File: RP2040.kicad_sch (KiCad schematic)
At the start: 26 parts, among them J3 Conn_01x02, J6 USB_B_Micro, U2 XC6206P332MR, U6 W25Q128JVS, U7 RP2040, Y1 X322512MSB4SI

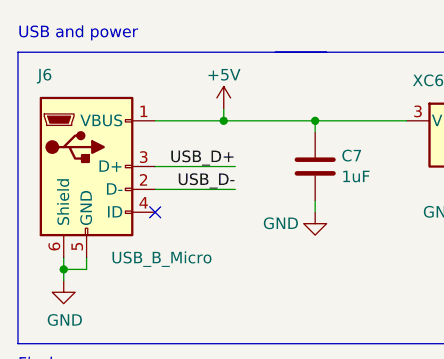
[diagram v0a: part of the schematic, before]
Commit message: Cleanup silkscreen and version/date
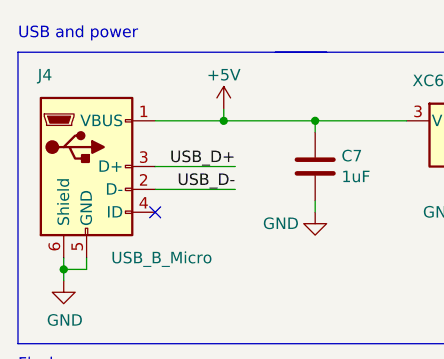
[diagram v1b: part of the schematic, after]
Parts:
- renumbered J6 to J4
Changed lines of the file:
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@@
   (paper "A4")
   (title_block
-    (date "${DATE}")
-    (rev "${VERSION}")
+    (date "${date}")
+    (rev "${version}")
   )
   (junction (at 215.9 20.32) (diameter 0) (color 0 0 0 0)
@@
   (symbol (lib_id "Connector:USB_B_Micro") (at 22.225 29.845 0) (unit 1)
     (in_bom yes) (on_board yes)
-    (property "Reference" "J6" (id 0) (at 18.415 19.685 0)
+    (property "Reference" "J4" (id 0) (at 18.415 19.685 0)
       (effects (font (size 1.27 1.27)) (justify right))
     )

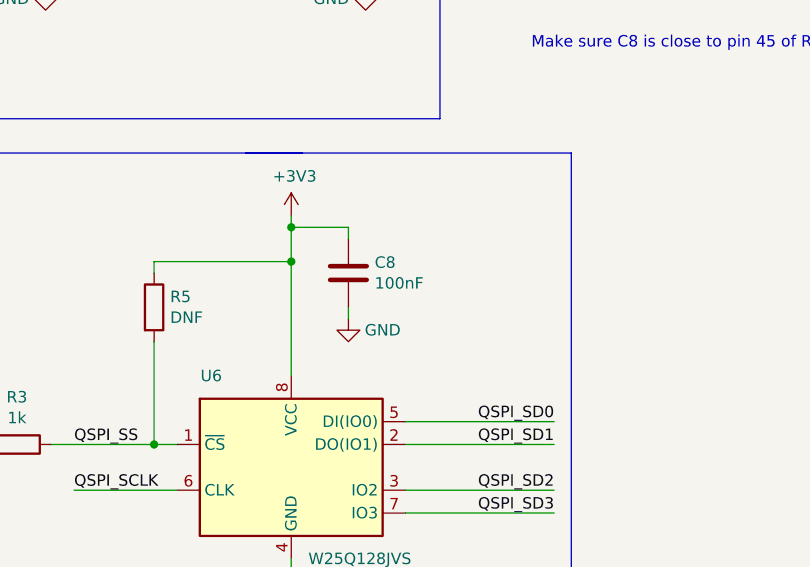
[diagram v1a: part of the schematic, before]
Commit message: Silkscreen and date/version stuff
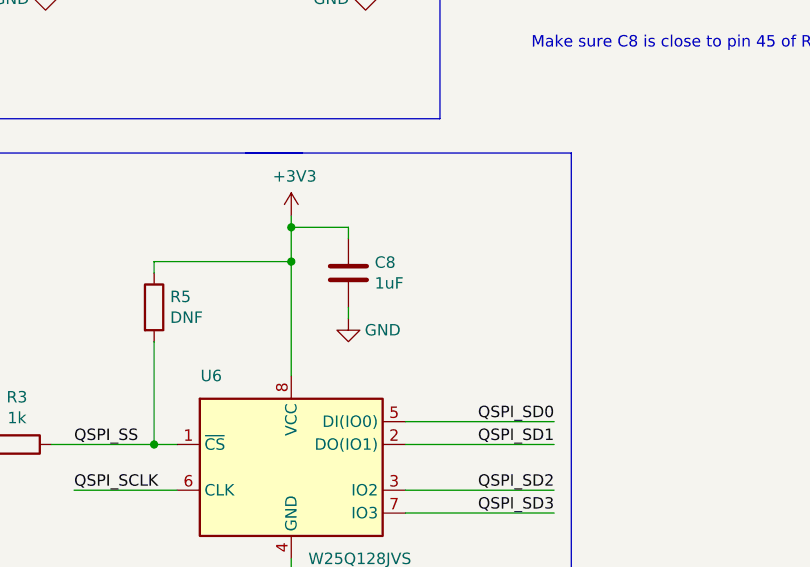
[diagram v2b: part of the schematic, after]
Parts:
- C10, C11, C12, C13, C15, C16, C17, C18, C19, C20: LCSC (none) -> C52923
- C7, C9: footprint Capacitor_SMD:C_0603_1608Metric -> Custom_Footprints:Perfect_0402; JLC 0603 -> 0402; LCSC C19702 -> C52923
- C8: value 100nF -> 1uF; LCSC C1525 -> C52923
- U6: JLC SOIC-8_5.3x5.3x1.27P -> SOIC-8-208mil
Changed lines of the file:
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@@
   (paper "A4")
   (title_block
-    (date "${date}")
-    (rev "${version}")
+    (date "${DATE}")
+    (rev "${VERSION}")
   )
   (junction (at 215.9 20.32) (diameter 0) (color 0 0 0 0)
@@
       (effects (font (size 1.27 1.27)) hide)
     )
-    (property "LCSC" "" (id 5) (at 149.86 25.4 0)
+    (property "LCSC" "C52923" (id 5) (at 149.86 25.4 0)
       (effects (font (size 1.27 1.27)) hide)
     )
@@
       (effects (font (size 1.27 1.27)) hide)
     )
-    (property "LCSC" "" (id 5) (at 149.86 40.64 0)
+    (property "LCSC" "C52923" (id 5) (at 149.86 40.64 0)
       (effects (font (size 1.27 1.27)) hide)
     )
@@
       (effects (font (size 1.27 1.27)) (justify left))
     )
-    (property "Footprint" "Capacitor_SMD:C_0603_1608Metric" (id 2) (at 84.1502 33.655 0)
+    (property "Footprint" "Custom_Footprints:Perfect_0402" (id 2) (at 84.1502 33.655 0)
       (effects (font (size 1.27 1.27)) hide)
     )
@@
       (effects (font (size 1.27 1.27)) hide)
     )
-    (property "JLC" "0603" (id 4) (at 83.185 29.845 0)
-      (effects (font (size 1.27 1.27)) hide)
-    )
-    (property "LCSC" "C19702" (id 5) (at 83.185 29.845 0)
+    (property "JLC" "0402" (id 4) (at 83.185 29.845 0)
+      (effects (font (size 1.27 1.27)) hide)
+    )
+    (property "LCSC" "C52923" (id 5) (at 83.185 29.845 0)
       (effects (font (size 1.27 1.27)) hide)
     )
@@
       (effects (font (size 1.27 1.27)) (justify left))
     )
-    (property "Value" "100nF" (id 1) (at 84.201 67.818 0)
+    (property "Value" "1uF" (id 1) (at 84.201 67.818 0)
       (effects (font (size 1.27 1.27)) (justify left))
     )
@@
       (effects (font (size 1.27 1.27)) hide)
     )
-    (property "LCSC" "C1525" (id 5) (at 81.28 66.675 0)
+    (property "LCSC" "C52923" (id 5) (at 81.28 66.675 0)
       (effects (font (size 1.27 1.27)) hide)
     )
@@
       (effects (font (size 1.27 1.27)) hide)
     )
-    (property "LCSC" "" (id 5) (at 250.19 25.4 0)
+    (property "LCSC" "C52923" (id 5) (at 250.19 25.4 0)
       (effects (font (size 1.27 1.27)) hide)
     )
@@
       (effects (font (size 1.27 1.27)) hide)
     )
-    (property "LCSC" "" (id 5) (at 238.76 25.4 0)
+    (property "LCSC" "C52923" (id 5) (at 238.76 25.4 0)
       (effects (font (size 1.27 1.27)) hide)
     )
@@
       (effects (font (size 1.27 1.27)) hide)
     )
-    (property "LCSC" "" (id 5) (at 273.05 25.4 0)
+    (property "LCSC" "C52923" (id 5) (at 273.05 25.4 0)
       (effects (font (size 1.27 1.27)) hide)
     )
@@
       (effects (font (size 1.27 1.27)) hide)
     )
-    (property "LCSC" "" (id 5) (at 215.9 25.4 0)
+    (property "LCSC" "C52923" (id 5) (at 215.9 25.4 0)
       (effects (font (size 1.27 1.27)) hide)
     )
@@
       (effects (font (size 1.27 1.27)) hide)
     )
-    (property "LCSC" "" (id 5) (at 227.33 25.4 0)
+    (property "LCSC" "C52923" (id 5) (at 227.33 25.4 0)
       (effects (font (size 1.27 1.27)) hide)
     )
@@
       (effects (font (size 1.27 1.27)) hide)
     )
-    (property "LCSC" "" (id 5) (at 261.62 25.4 0)
+    (property "LCSC" "C52923" (id 5) (at 261.62 25.4 0)
       (effects (font (size 1.27 1.27)) hide)
     )
@@
       (effects (font (size 1.27 1.27)) hide)
     )
-    (property "JLC" "SOIC-8_5.3x5.3x1.27P" (id 4) (at 74.93 88.265 0)
+    (property "JLC" "SOIC-8-208mil" (id 4) (at 74.93 88.265 0)
       (effects (font (size 1.27 1.27)) hide)
     )
@@
       (effects (font (size 1.27 1.27)) (justify left))
     )
-    (property "Footprint" "Capacitor_SMD:C_0603_1608Metric" (id 2) (at 48.5902 33.655 0)
+    (property "Footprint" "Custom_Footprints:Perfect_0402" (id 2) (at 48.5902 33.655 0)
       (effects (font (size 1.27 1.27)) hide)
     )
@@
       (effects (font (size 1.27 1.27)) hide)
     )
-    (property "JLC" "0603" (id 4) (at 47.625 29.845 0)
-      (effects (font (size 1.27 1.27)) hide)
-    )
-    (property "LCSC" "C19702" (id 5) (at 47.625 29.845 0)
+    (property "JLC" "0402" (id 4) (at 47.625 29.845 0)
+      (effects (font (size 1.27 1.27)) hide)
+    )
+    (property "LCSC" "C52923" (id 5) (at 47.625 29.845 0)
       (effects (font (size 1.27 1.27)) hide)
     )
@@
       (effects (font (size 1.27 1.27)) hide)
     )
-    (property "LCSC" "" (id 5) (at 204.47 25.4 0)
+    (property "LCSC" "C52923" (id 5) (at 204.47 25.4 0)
       (effects (font (size 1.27 1.27)) hide)
     )
@@
       (effects (font (size 1.27 1.27)) hide)
     )
-    (property "LCSC" "" (id 5) (at 138.43 25.4 0)
-      (effects (font (size 1.27 1.27)) hide)
-    )
+    (property "LCSC" "C52923" (id 5) (at 138.43 25.4 0)
+      (effects (font (size 1.27 1.27)) hide)
+    )

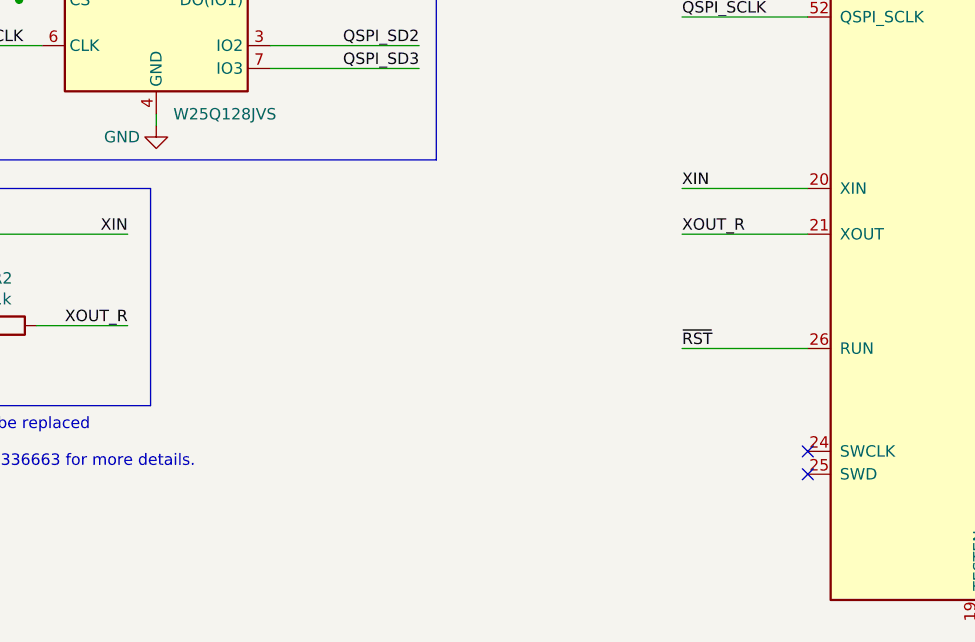
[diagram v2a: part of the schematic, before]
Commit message: Add debug connections
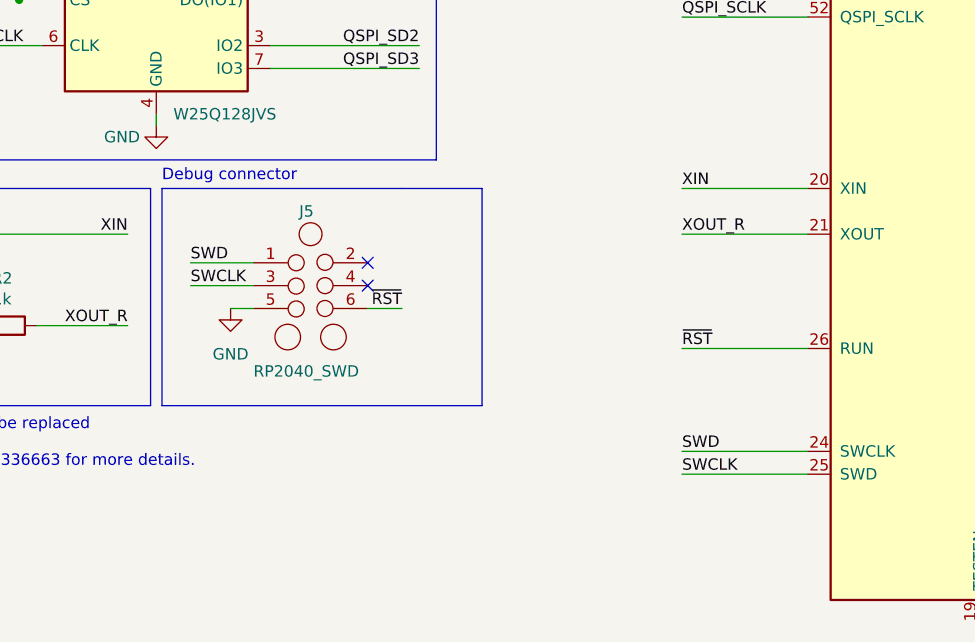
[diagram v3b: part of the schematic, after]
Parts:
- added J5: RP2040_SWD, Connector:Tag-Connect_TC2030-IDC-NL_2x03_P1.27mm_Vertical, symbol Custom_Symbols:TC2030-IDC-NL
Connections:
- net GND: now also J5.5 (Pin_5)
- net ~{RST}: now also J5.6 (Pin_6)
- net SWD: now reaches U7.24 (SWCLK)
- net SWD: now also J5.1 (Pin_1)
- net SWCLK: now reaches U7.25 (SWD)
- net SWCLK: now also J5.3 (Pin_3)
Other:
- note added: "Debug connector"
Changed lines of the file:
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@@
   )
   (no_connect (at 29.845 34.925))
-  (no_connect (at 147.32 138.43))
-  (no_connect (at 147.32 135.89))
+  (no_connect (at 98.425 117.475))
+  (no_connect (at 98.425 114.935))
   (wire (pts (xy 138.43 20.32) (xy 149.86 20.32))
     (stroke (width 0) (type default) (color 0 0 0 0))
@@
     (stroke (width 0) (type default) (color 0 0 0 0))
   )
+  (wire (pts (xy 78.74 114.935) (xy 85.725 114.935))
+    (stroke (width 0) (type default) (color 0 0 0 0))
+  )
   (wire (pts (xy 210.82 73.66) (xy 226.06 73.66))
     (stroke (width 0) (type default) (color 0 0 0 0))
@@
     (stroke (width 0) (type default) (color 0 0 0 0))
   )
+  (polyline (pts (xy 75.565 106.68) (xy 75.565 130.81))
+    (stroke (width 0) (type default) (color 0 0 0 0))
+  )
   (wire (pts (xy 81.28 61.595) (xy 74.93 61.595))
     (stroke (width 0) (type default) (color 0 0 0 0))
@@
     (stroke (width 0) (type default) (color 0 0 0 0))
   )
+  (polyline (pts (xy 111.125 106.68) (xy 111.125 130.81))
+    (stroke (width 0) (type default) (color 0 0 0 0))
+  )
   (wire (pts (xy 29.845 24.765) (xy 37.465 24.765))
     (stroke (width 0) (type default) (color 0 0 0 0))
@@
     (stroke (width 0) (type default) (color 0 0 0 0))
   )
+  (wire (pts (xy 78.74 117.475) (xy 85.725 117.475))
+    (stroke (width 0) (type default) (color 0 0 0 0))
+  )
   (wire (pts (xy 133.35 83.82) (xy 147.32 83.82))
     (stroke (width 0) (type default) (color 0 0 0 0))
@@
     (stroke (width 0) (type default) (color 0 0 0 0))
   )
+  (polyline (pts (xy 111.125 130.81) (xy 102.235 130.81))
+    (stroke (width 0) (type default) (color 0 0 0 0))
+  )
   (wire (pts (xy 59.69 66.675) (xy 59.69 65.405))
     (stroke (width 0) (type default) (color 0 0 0 0))
   )
+  (wire (pts (xy 83.185 120.015) (xy 85.725 120.015))
+    (stroke (width 0) (type default) (color 0 0 0 0))
+  )
   (wire (pts (xy 215.9 21.59) (xy 215.9 20.32))
     (stroke (width 0) (type default) (color 0 0 0 0))
@@
     (stroke (width 0) (type default) (color 0 0 0 0))
   )
+  (wire (pts (xy 133.35 135.89) (xy 147.32 135.89))
+    (stroke (width 0) (type default) (color 0 0 0 0))
+  )
   (wire (pts (xy 22.225 41.275) (xy 19.685 41.275))
     (stroke (width 0) (type default) (color 0 0 0 0))
   )
+  (polyline (pts (xy 102.235 106.68) (xy 111.125 106.68))
+    (stroke (width 0) (type default) (color 0 0 0 0))
+  )
   (wire (pts (xy 238.76 20.32) (xy 250.19 20.32))
     (stroke (width 0) (type default) (color 0 0 0 0))
@@
     (stroke (width 0) (type default) (color 0 0 0 0))
   )
+  (polyline (pts (xy 75.565 106.68) (xy 102.235 106.68))
+    (stroke (width 0) (type default) (color 0 0 0 0))
+  )
   (wire (pts (xy 138.43 30.48) (xy 149.86 30.48))
     (stroke (width 0) (type default) (color 0 0 0 0))
@@
     (stroke (width 0) (type default) (color 0 0 0 0))
   )
+  (wire (pts (xy 98.425 120.015) (xy 102.235 120.015))
+    (stroke (width 0) (type default) (color 0 0 0 0))
+  )
   (polyline (pts (xy 106.045 103.505) (xy 106.045 53.34))
     (stroke (width 0) (type default) (color 0 0 0 0))
@@
     (stroke (width 0) (type default) (color 0 0 0 0))
   )
+  (polyline (pts (xy 75.565 130.81) (xy 102.235 130.81))
+    (stroke (width 0) (type default) (color 0 0 0 0))
+  )
   (wire (pts (xy 204.47 21.59) (xy 204.47 20.32))
     (stroke (width 0) (type default) (color 0 0 0 0))
@@
   )
   (wire (pts (xy 273.05 31.75) (xy 273.05 33.02))
+    (stroke (width 0) (type default) (color 0 0 0 0))
+  )
+  (wire (pts (xy 133.35 138.43) (xy 147.32 138.43))
     (stroke (width 0) (type default) (color 0 0 0 0))
   )
@@
     (effects (font (size 1.27 1.27)) (justify left bottom))
   )
+  (text "Debug connector" (at 75.565 106.045 0)
+    (effects (font (size 1.27 1.27)) (justify left bottom))
+  )
   (text "Make sure C8 is close to pin 45 of RP2040" (at 101.6 41.91 0)
+    (effects (font (size 1.27 1.27)) (justify left bottom))
+  )
+  (label "SWD" (at 133.35 135.89 0)
     (effects (font (size 1.27 1.27)) (justify left bottom))
   )
@@
     (effects (font (size 1.27 1.27)) (justify left bottom))
   )
+  (label "SWCLK" (at 78.74 117.475 0)
+    (effects (font (size 1.27 1.27)) (justify left bottom))
+  )
   (label "QSPI_SD1" (at 133.35 78.74 0)
     (effects (font (size 1.27 1.27)) (justify left bottom))
@@
     (effects (font (size 1.27 1.27)) (justify left bottom))
   )
+  (label "~{RST}" (at 102.235 120.015 180)
+    (effects (font (size 1.27 1.27)) (justify right bottom))
+  )
   (label "USB_D-" (at 38.735 32.385 180)
     (effects (font (size 1.27 1.27)) (justify right bottom))
@@
     (effects (font (size 1.27 1.27)) (justify right bottom))
   )
+  (label "SWD" (at 78.74 114.935 0)
+    (effects (font (size 1.27 1.27)) (justify left bottom))
+  )
   (label "XOUT_R" (at 133.35 111.76 0)
     (effects (font (size 1.27 1.27)) (justify left bottom))
@@
   )
   (label "XIN" (at 133.35 106.68 0)
+    (effects (font (size 1.27 1.27)) (justify left bottom))
+  )
+  (label "SWCLK" (at 133.35 138.43 0)
     (effects (font (size 1.27 1.27)) (justify left bottom))
   )
@@
     (pin "2")
   )
+  (symbol (lib_id "Custom_Symbols:TC2030-IDC-NL") (at 92.075 117.475 0) (unit 1)
+    (in_bom yes) (on_board yes)
+    (property "Reference" "J5" (id 0) (at 90.805 109.22 0)
+      (effects (font (size 1.27 1.27)) (justify left))
+    )
+    (property "Value" "RP2040_SWD" (id 1) (at 85.725 127 0)
+      (effects (font (size 1.27 1.27)) (justify left))
+    )
+    (property "Footprint" "Connector:Tag-Connect_TC2030-IDC-NL_2x03_P1.27mm_Vertical" (id 2) (at 90.805 117.475 0)
+      (effects (font (size 1.27 1.27)) hide)
+    )
+    (property "Datasheet" "https://www.tag-connect.com/wp-content/uploads/bsk-pdf-manager/2019/12/TC2030-IDC-NL-Datasheet-Rev-B.pdf" (id 3) (at 92.075 131.445 0)
+      (effects (font (size 1.27 1.27)) hide)
+    )
+    (pin "1")
+    (pin "2")
+    (pin "3")
+    (pin "4")
+    (pin "5")
+    (pin "6")
+  )
   (symbol (lib_id "power:+3V3") (at 195.58 19.05 0) (unit 1)
     (in_bom yes) (on_board yes)
@@
     (pin "8")
   )
+  (symbol (lib_id "power:GND") (at 83.185 120.015 0) (unit 1)
+    (in_bom yes) (on_board yes) (fields_autoplaced)
+    (property "Reference" "#PWR0116" (id 0) (at 83.185 126.365 0)
+      (effects (font (size 1.27 1.27)) hide)
+    )
+    (property "Value" "GND" (id 1) (at 83.185 125.095 0))
+    (property "Footprint" "" (id 2) (at 83.185 120.015 0)
+      (effects (font (size 1.27 1.27)) hide)
+    )
+    (property "Datasheet" "" (id 3) (at 83.185 120.015 0)
+      (effects (font (size 1.27 1.27)) hide)
+    )
+    (pin "1")
+  )
   (symbol (lib_id "Device:C") (at 47.625 29.845 0) (unit 1)

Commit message: Final changes prior to ordering
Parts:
- removed U2: XC6206P332MR, Package_TO_SOT_SMD:SOT-23, symbol Regulator_Linear:XC6206PxxxMR
- added U2: AMS1117-3.3, Package_TO_SOT_SMD:SOT-223-3_TabPin2, symbol Regulator_Linear:AMS1117-3.3
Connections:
- net +3V3: now also U2.2 (VO)
- net +5V: now also U2.3 (VI)
- net GND: now also U2.1 (GND)
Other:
- note added: "Make sure one of these is close to pin 45 of RP2040"
- note removed: "Make sure C8 is close to pin 45 of RP2040"
- note removed: "Make sure R3 and R4 are close to RP2040"
- moved on the sheet: C10, C11, C12
